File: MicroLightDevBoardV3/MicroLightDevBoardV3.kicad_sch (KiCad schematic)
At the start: 30 parts, among them J1 TYPE-C-31-M-12, J2 Conn_01x02_Socket, J3 Conn_01x03_Socket, J4 Conn_01x01_Socket, J5 Conn_01x01_Socket, SW1 SW_Push, U1 USBLC6-2P6, U2 STM32C071GBUx, U3 BQ25180, U4 S-85S1AB33-I6T1U, U7 MC3479

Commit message: add battery connector
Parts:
- added U5: DF53-2S-0.6H, MicroLightDevBoard:DF53-2S-0.6H, symbol MicroLightDevBoard:DF53-2S-0.6H
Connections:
- net BAT_CHRG: now also U5.1
- net GND: now also J2.2 (Pin_2), U5.2; no longer R1.2
- net bulbLed: now also R1.2; no longer J2.1 (Pin_1)
- net at R1.1: now also J2.1 (Pin_1); no longer J2.2 (Pin_2)
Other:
- moved on the sheet: J4, J5, R1
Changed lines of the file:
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@@
 	(wire
 		(pts
-			(xy 35.56 177.8) (xy 46.99 177.8)
+			(xy 118.11 172.72) (xy 132.08 172.72)
 		)
 		(stroke
@@
 	(wire
 		(pts
-			(xy 118.11 172.72) (xy 132.08 172.72)
+			(xy 222.25 109.22) (xy 229.87 109.22)
 		)
 		(stroke
@@
 	(wire
 		(pts
-			(xy 222.25 109.22) (xy 229.87 109.22)
+			(xy 220.98 109.22) (xy 222.25 109.22)
 		)
 		(stroke
@@
 	(wire
 		(pts
-			(xy 220.98 109.22) (xy 222.25 109.22)
+			(xy 227.33 58.42) (xy 232.41 58.42)
 		)
 		(stroke
@@
 	(wire
 		(pts
-			(xy 227.33 58.42) (xy 232.41 58.42)
+			(xy 41.91 43.18) (xy 53.34 43.18)
 		)
 		(stroke
@@
 	(wire
 		(pts
-			(xy 41.91 43.18) (xy 53.34 43.18)
+			(xy 27.94 177.8) (xy 46.99 177.8)
 		)
 		(stroke
@@
 	(wire
 		(pts
+			(xy 27.94 175.26) (xy 39.37 175.26)
+		)
+		(stroke
+			(width 0)
+			(type default)
+		)
+	)
+	(wire
+		(pts
 			(xy 130.81 101.6) (xy 133.35 101.6)
 		)
@@
 		)
 	)
+	(global_label "BAT_CHRG"
+		(shape input)
+		(at 154.94 158.75 180)
+		(fields_autoplaced yes)
+		(effects
+			(font
+				(size 1.27 1.27)
+			)
+			(justify right)
+		)
+		(property "Intersheetrefs" "${INTERSHEET_REFS}"
+			(at 142.5205 158.75 0)
+			(effects
+				(font
+					(size 1.27 1.27)
+				)
+				(justify right)
+				(hide yes)
+			)
+		)
+	)
 	(global_label "I2C_SCL"
 		(shape input)
@@
 	(global_label "BAT_CHRG"
 		(shape input)
-		(at 87.63 191.77 180)
+		(at 203.2 158.75 180)
 		(fields_autoplaced yes)
 		(effects
@@
 		)
 		(property "Intersheetrefs" "${INTERSHEET_REFS}"
-			(at 75.2105 191.77 0)
+			(at 190.7805 158.75 0)
 			(effects
 				(font
@@
 	(global_label "bulbLed"
 		(shape input)
-		(at 46.99 175.26 180)
+		(at 27.94 175.26 180)
 		(fields_autoplaced yes)
 		(effects
@@
 		)
 		(property "Intersheetrefs" "${INTERSHEET_REFS}"
-			(at 36.6269 175.26 0)
+			(at 17.5769 175.26 0)
 			(effects
 				(font
@@
 	(symbol
 		(lib_id "Connector:Conn_01x01_Socket")
-		(at 92.71 191.77 0)
+		(at 208.28 158.75 0)
 		(unit 1)
 		(exclude_from_sim no)
@@
 		(fields_autoplaced yes)
 		(property "Reference" "J4"
-			(at 93.98 190.4999 0)
+			(at 209.55 157.4799 0)
 			(effects
 				(font
@@
 		)
 		(property "Value" "Conn_01x01_Socket"
-			(at 93.98 193.0399 0)
+			(at 209.55 160.0199 0)
 			(effects
 				(font
@@
 		)
 		(property "Footprint" "MicroLightDevBoard:battery_1x01_Vertical"
-			(at 92.71 191.77 0)
+			(at 208.28 158.75 0)
 			(effects
 				(font
@@
 		)
 		(property "Datasheet" "~"
-			(at 92.71 191.77 0)
+			(at 208.28 158.75 0)
 			(effects
 				(font
@@
 		)
 		(property "Description" "Generic connector, single row, 01x01, script generated"
-			(at 92.71 191.77 0)
+			(at 208.28 158.75 0)
 			(effects
 				(font
@@
 	(symbol
 		(lib_id "Connector:Conn_01x01_Socket")
-		(at 92.71 182.88 0)
+		(at 208.28 149.86 0)
 		(unit 1)
 		(exclude_from_sim no)
@@
 		(fields_autoplaced yes)
 		(property "Reference" "J5"
-			(at 93.98 181.6099 0)
+			(at 209.55 148.5899 0)
 			(effects
 				(font
@@
 		)
 		(property "Value" "Conn_01x01_Socket"
-			(at 93.98 184.1499 0)
+			(at 209.55 151.1299 0)
 			(effects
 				(font
@@
 		)
 		(property "Footprint" "MicroLightDevBoard:battery_1x01_Vertical"
-			(at 92.71 182.88 0)
+			(at 208.28 149.86 0)
 			(effects
 				(font
@@
 		)
 		(property "Datasheet" "~"
-			(at 92.71 182.88 0)
+			(at 208.28 149.86 0)
 			(effects
 				(font
@@
 		)
 		(property "Description" "Generic connector, single row, 01x01, script generated"
-			(at 92.71 182.88 0)
+			(at 208.28 149.86 0)
 			(effects
 				(font
@@
 	(symbol
 		(lib_id "Device:R")
-		(at 31.75 177.8 270)
+		(at 43.18 175.26 270)
 		(unit 1)
 		(exclude_from_sim no)
@@
 		(dnp no)
 		(property "Reference" "R1"
-			(at 31.75 171.45 90)
+			(at 43.18 168.91 90)
 			(effects
 				(font
@@
 		)
 		(property "Value" "51"
-			(at 31.75 173.99 90)
+			(at 43.18 171.45 90)
 			(effects
 				(font
@@
 		)
 		(property "Footprint" "Resistor_SMD:R_0402_1005Metric"
-			(at 31.75 176.022 90)
+			(at 43.18 173.482 90)
 			(effects
 				(font
@@
 		)
 		(property "Datasheet" "~"
-			(at 31.75 177.8 0)
+			(at 43.18 175.26 0)
 			(effects
 				(font
@@
 		)
 		(property "Description" "Resistor"
-			(at 31.75 177.8 0)
+			(at 43.18 175.26 0)
 			(effects
 				(font
@@
 	(symbol
 		(lib_id "power:GND")
-		(at 87.63 182.88 270)
+		(at 203.2 149.86 270)
 		(unit 1)
 		(exclude_from_sim no)
@@
 		(fields_autoplaced yes)
 		(property "Reference" "#PWR024"
-			(at 81.28 182.88 0)
+			(at 196.85 149.86 0)
 			(effects
 				(font
@@
 		)
 		(property "Value" "GND"
-			(at 83.82 182.8799 90)
+			(at 199.39 149.8599 90)
 			(effects
 				(font
@@
 		)
 		(property "Footprint" ""
-			(at 87.63 182.88 0)
+			(at 203.2 149.86 0)
 			(effects
 				(font
@@
 		)
 		(property "Datasheet" ""
-			(at 87.63 182.88 0)
+			(at 203.2 149.86 0)
 			(effects
 				(font
@@
 		)
 		(property "Description" "Power symbol creates a global label with name \"GND\" , ground"
-			(at 87.63 182.88 0)
+			(at 203.2 149.86 0)
 			(effects
 				(font
@@
 	(symbol
 		(lib_id "power:GND")
+		(at 154.94 161.29 270)
+		(unit 1)
+		(exclude_from_sim no)
+		(in_bom yes)
+		(on_board yes)
+		(dnp no)
+		(fields_autoplaced yes)
+		(property "Reference" "#PWR029"
+			(at 148.59 161.29 0)
+			(effects
+				(font
+					(size 1.27 1.27)
+				)
+				(hide yes)
+			)
+		)
+		(property "Value" "GND"
+			(at 151.13 161.2899 90)
+			(effects
+				(font
+					(size 1.27 1.27)
+				)
+				(justify right)
+			)
+		)
+		(property "Footprint" ""
+			(at 154.94 161.29 0)
+			(effects
+				(font
+					(size 1.27 1.27)
+				)
+				(hide yes)
+			)
+		)
+		(property "Datasheet" ""
+			(at 154.94 161.29 0)
+			(effects
+				(font
+					(size 1.27 1.27)
+				)
+				(hide yes)
+			)
+		)
+		(property "Description" "Power symbol creates a global label with name \"GND\" , ground"
+			(at 154.94 161.29 0)
+			(effects
+				(font
+					(size 1.27 1.27)
+				)
+				(hide yes)
+			)
+		)
+		(pin "1"
+		)
+		(instances
+			(project "MicroLightDevBoardV3"
+				(path "/9009d70b-273c-45fe-8624-596a22a35a49"
+					(reference "#PWR029")
+					(unit 1)
+				)
+			)
+		)
+	)
+	(symbol
+		(lib_id "power:GND")
 		(at 49.53 33.02 90)
 		(unit 1)
@@
 					(unit 1)
 				)
+			)
+		)
+	)
+	(symbol
+		(lib_id "MicroLightDevBoard:DF53-2S-0.6H")
+		(at 161.29 156.21 0)
+		(unit 1)
+		(exclude_from_sim no)
+		(in_bom yes)
+		(on_board yes)
+		(dnp no)
+		(fields_autoplaced yes)
+		(property "Reference" "U5"
+			(at 168.91 158.7499 0)
+			(effects
+				(font
+					(size 1.27 1.27)
+				)
+				(justify left)
+			)
+		)
+		(property "Value" "DF53-2S-0.6H"
+			(at 168.91 161.2899 0)
+			(effects
+				(font
+					(size 1.27 1.27)
+				)
+				(justify left)
+			)
+		)
+		(property "Footprint" "MicroLightDevBoard:DF53-2S-0.6H"
+			(at 161.29 156.21 0)
+			(effects
+				(font
+					(size 1.27 1.27)
+				)
+				(hide yes)
+			)
+		)
+		(property "Datasheet" "https://www.hirose.com/en/product/document?clcode=CL0668-1007-0-00&productname=DF53-10S-0.6H&series=DF53&documenttype=Catalog&lang=en&documentid=en_DF53_CAT"
+			(at 161.29 156.21 0)
+			(effects
+				(font
+					(size 1.27 1.27)
+				)
+				(hide yes)
+			)
+		)
+		(property "Description" ""
+			(at 161.29 156.21 0)
+			(effects
+				(font
+					(size 1.27 1.27)
+				)
+				(hide yes)
+			)
+		)
+		(pin "4"
+		)
+		(pin "3"
+		)
+		(pin "1"
+		)
+		(pin "2"
+		)
+		(instances
+			(project ""
+				(path "/9009d70b-273c-45fe-8624-596a22a35a49"
+					(reference "U5")
+					(unit 1)
+				)

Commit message: lcsc ids, adjust footprints, cleanup
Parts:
- C1, C8: LCSC (none) -> C1525
- C2: LCSC (none) -> C23733
- R1, R6: LCSC (none) -> C25125
- R4, R5, R9: LCSC (none) -> C25744
- R7, R8: LCSC (none) -> C270617
- U2: LCSC (none) -> C42240018; LSCS C42240018 -> (none)
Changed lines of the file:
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@@
 			)
 		)
+		(property "LCSC" "C25125"
+			(at 43.18 175.26 90)
+			(effects
+				(font
+					(size 1.27 1.27)
+				)
+				(hide yes)
+			)
+		)
 		(pin "1"
 		)
@@
 			)
 		)
+		(property "LCSC" "C1525"
+			(at 97.79 21.59 90)
+			(effects
+				(font
+					(size 1.27 1.27)
+				)
+				(hide yes)
+			)
+		)
 		(pin "2"
 		)
@@
 			)
 		)
+		(property "LCSC" "C25744"
+			(at 132.08 130.81 90)
+			(effects
+				(font
+					(size 1.27 1.27)
+				)
+				(hide yes)
+			)
+		)
 		(pin "1"
 		)
@@
 			)
 		)
+		(property "LCSC" "C270617"
+			(at 66.04 128.27 90)
+			(effects
+				(font
+					(size 1.27 1.27)
+				)
+				(hide yes)
+			)
+		)
 		(pin "2"
 		)
@@
 			)
 		)
-		(property "Field5" ""
+		(property "LCSC" "C23733"
 			(at 97.79 26.67 90)
 			(effects
@@
 			)
 		)
+		(property "LCSC" "C270617"
+			(at 66.04 133.35 90)
+			(effects
+				(font
+					(size 1.27 1.27)
+				)
+				(hide yes)
+			)
+		)
 		(pin "2"
 		)
@@
 			)
 		)
+		(property "LCSC" "C25744"
+			(at 57.15 86.36 90)
+			(effects
+				(font
+					(size 1.27 1.27)
+				)
+				(hide yes)
+			)
+		)
 		(pin "1"
 		)
@@
 			)
 		)
+		(property "LCSC" "C25744"
+			(at 57.15 76.2 90)
+			(effects
+				(font
+					(size 1.27 1.27)
+				)
+				(hide yes)
+			)
+		)
 		(pin "1"
 		)
@@
 			)
 		)
-		(property "LSCS" "C42240018"
+		(property "LCSC" "C42240018"
 			(at 104.14 55.88 0)
 			(effects
@@
 			)
 		)
+		(property "LCSC" "C25125"
+			(at 66.04 123.19 90)
+			(effects
+				(font
+					(size 1.27 1.27)
+				)
+				(hide yes)
+			)
+		)
 		(pin "2"
 		)
@@
 			(at 222.25 113.03 0)
 			(effects
+				(font
+					(size 1.27 1.27)
+				)
+				(hide yes)
+			)
+		)
+		(property "LCSC" "C1525"
+			(at 222.25 113.03 0)
+			(effects

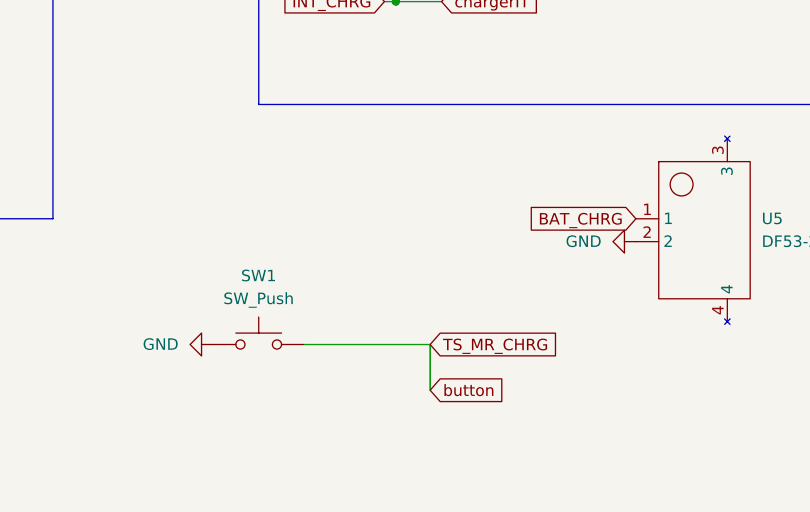
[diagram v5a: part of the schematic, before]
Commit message: add pullup resistor on button, internal mcu pullup not enough because of charging ic pulses
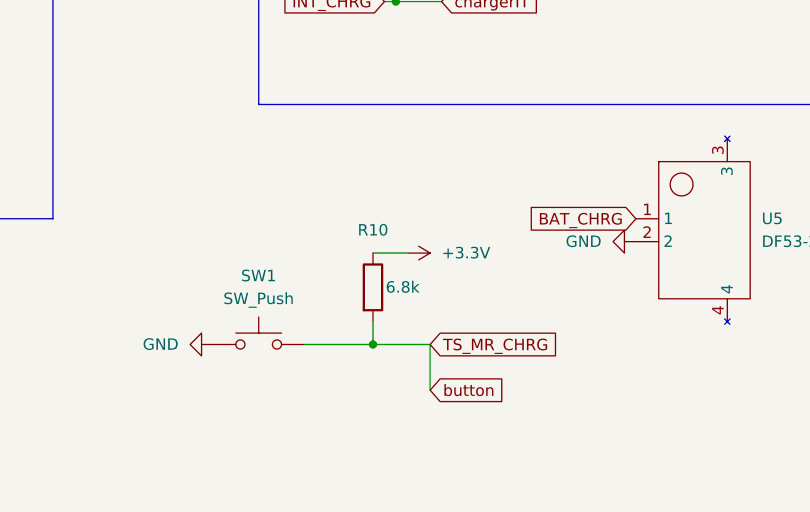
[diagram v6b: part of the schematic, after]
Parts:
- added R10: 6.8k, Resistor_SMD:R_0402_1005Metric, symbol Device:R
- U2: LCSC C42240018 -> C42113261
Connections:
- net +3.3V: now also R10.1
- net TS_MR_CHRG: now also R10.2
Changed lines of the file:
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@@
 	)
 	(junction
+		(at 125.73 172.72)
+		(diameter 0)
+		(color 0 0 0 0)
+	)
+	(junction
 		(at 172.72 101.6)
 		(diameter 0)
@@
 	(wire
 		(pts
+			(xy 125.73 172.72) (xy 132.08 172.72)
+		)
+		(stroke
+			(width 0)
+			(type default)
+		)
+	)
+	(wire
+		(pts
 			(xy 186.69 67.31) (xy 186.69 60.96)
 		)
@@
 	(wire
 		(pts
-			(xy 118.11 172.72) (xy 132.08 172.72)
+			(xy 118.11 172.72) (xy 125.73 172.72)
+		)
+		(stroke
+			(width 0)
+			(type default)
+		)
+	)
+	(wire
+		(pts
+			(xy 125.73 170.18) (xy 125.73 172.72)
 		)
 		(stroke
@@
 	(wire
 		(pts
+			(xy 125.73 162.56) (xy 129.54 162.56)
+		)
+		(stroke
+			(width 0)
+			(type default)
+		)
+	)
+	(wire
+		(pts
 			(xy 27.94 177.8) (xy 46.99 177.8)
 		)
@@
 	)
 	(symbol
+		(lib_id "Device:R")
+		(at 125.73 166.37 0)
+		(unit 1)
+		(exclude_from_sim no)
+		(in_bom yes)
+		(on_board yes)
+		(dnp no)
+		(property "Reference" "R10"
+			(at 125.73 160.02 0)
+			(effects
+				(font
+					(size 1.27 1.27)
+				)
+			)
+		)
+		(property "Value" "6.8k"
+			(at 129.032 166.37 0)
+			(effects
+				(font
+					(size 1.27 1.27)
+				)
+			)
+		)
+		(property "Footprint" "Resistor_SMD:R_0402_1005Metric"
+			(at 123.952 166.37 90)
+			(effects
+				(font
+					(size 1.27 1.27)
+				)
+				(hide yes)
+			)
+		)
+		(property "Datasheet" "~"
+			(at 125.73 166.37 0)
+			(effects
+				(font
+					(size 1.27 1.27)
+				)
+				(hide yes)
+			)
+		)
+		(property "Description" "Resistor"
+			(at 125.73 166.37 0)
+			(effects
+				(font
+					(size 1.27 1.27)
+				)
+				(hide yes)
+			)
+		)
+		(property "LCSC" "C25744"
+			(at 125.73 166.37 90)
+			(effects
+				(font
+					(size 1.27 1.27)
+				)
+				(hide yes)
+			)
+		)
+		(pin "1"
+		)
+		(pin "2"
+		)
+		(instances
+			(project "MicroLightDevBoardV3"
+				(path "/9009d70b-273c-45fe-8624-596a22a35a49"
+					(reference "R10")
+					(unit 1)
+				)
+			)
+		)
+	)
+	(symbol
 		(lib_id "power:+3.3V")
 		(at 255.27 105.41 270)
@@
 			)
 		)
-		(property "LCSC" "C42240018"
+		(property "LCSC" "C42113261"
 			(at 104.14 55.88 0)
 			(effects
@@
 					(unit 1)
 				)
+			)
+		)
+	)
+	(symbol
+		(lib_id "power:+3.3V")
+		(at 129.54 162.56 270)
+		(unit 1)
+		(exclude_from_sim no)
+		(in_bom yes)
+		(on_board yes)
+		(dnp no)
+		(fields_autoplaced yes)
+		(property "Reference" "#PWR030"
+			(at 125.73 162.56 0)
+			(effects
+				(font
+					(size 1.27 1.27)
+				)
+				(hide yes)
+			)
+		)
+		(property "Value" "+3.3V"
+			(at 133.35 162.5599 90)
+			(effects
+				(font
+					(size 1.27 1.27)
+				)
+				(justify left)
+			)
+		)
+		(property "Footprint" ""
+			(at 129.54 162.56 0)
+			(effects
+				(font
+					(size 1.27 1.27)
+				)
+				(hide yes)
+			)
+		)
+		(property "Datasheet" ""
+			(at 129.54 162.56 0)
+			(effects
+				(font
+					(size 1.27 1.27)
+				)
+				(hide yes)
+			)
+		)
+		(property "Description" "Power symbol creates a global label with name \"+3.3V\""
+			(at 129.54 162.56 0)
+			(effects
+				(font
+					(size 1.27 1.27)
+				)
+				(hide yes)
+			)
+		)
+		(pin "1"
+		)
+		(instances
+			(project "MicroLightDevBoardV3"
+				(path "/9009d70b-273c-45fe-8624-596a22a35a49"
+					(reference "#PWR030")
+					(unit 1)
+				)

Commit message: removed incorrect lcsc part number
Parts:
- R10: LCSC C25744 -> (none)
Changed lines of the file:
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@@
-			)
-		)
-		(property "LCSC" "C25744"
-			(at 125.73 166.37 90)
-			(effects
-				(font
-					(size 1.27 1.27)
-				)
-				(hide yes)
 			)
 		)
